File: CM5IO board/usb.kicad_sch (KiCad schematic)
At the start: 0 parts

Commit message: Duplicated additional USB-C in sch.
How to change pin label on CM5?
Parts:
- added D5: SP0503BAHT, Package_TO_SOT_SMD:SOT-143, symbol Power_Protection:SP0503BAHT
- added J9: USB_C_Receptacle_USB2.0, iclr:USB_C_Receptacle_Palconn_UTC16-G, symbol Connector:USB_C_Receptacle_USB2.0
- added LED6: WHITE_LED, LED_SMD:LED_0402_1005Metric, symbol Device:LED_Small
- added R24, R25, R26: 5.1k, Resistor_SMD:R_0402_1005Metric, symbol Device:R_Small
- added TP6, TP7: TestPoint, TestPoint:TestPoint_Pad_D1.0mm, symbol Connector:TestPoint
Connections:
- new net: LED6.2 (A), R26.2
- new net: J9.B5 (CC2), R25.2
- new net: J9.A5 (CC1), R24.1
- new net Data+: D5.4 (K), J9.A6 (D+), J9.B6 (D+), TP7.1
- new net Data-: D5.3 (K), J9.A7 (D-), J9.B7 (D-), TP6.1
- new net GND: D5.1 (A), J9.A1 (GND), J9.A12 (GND), J9.B1 (GND), J9.B12 (GND), J9.S1 (SHIELD), LED6.1 (K), R24.2, R25.1
- new net VBUS: D5.2 (K), J9.A4 (VBUS), J9.A9 (VBUS), J9.B4 (VBUS), J9.B9 (VBUS), R26.1
- no-connect marks 0 -> 2

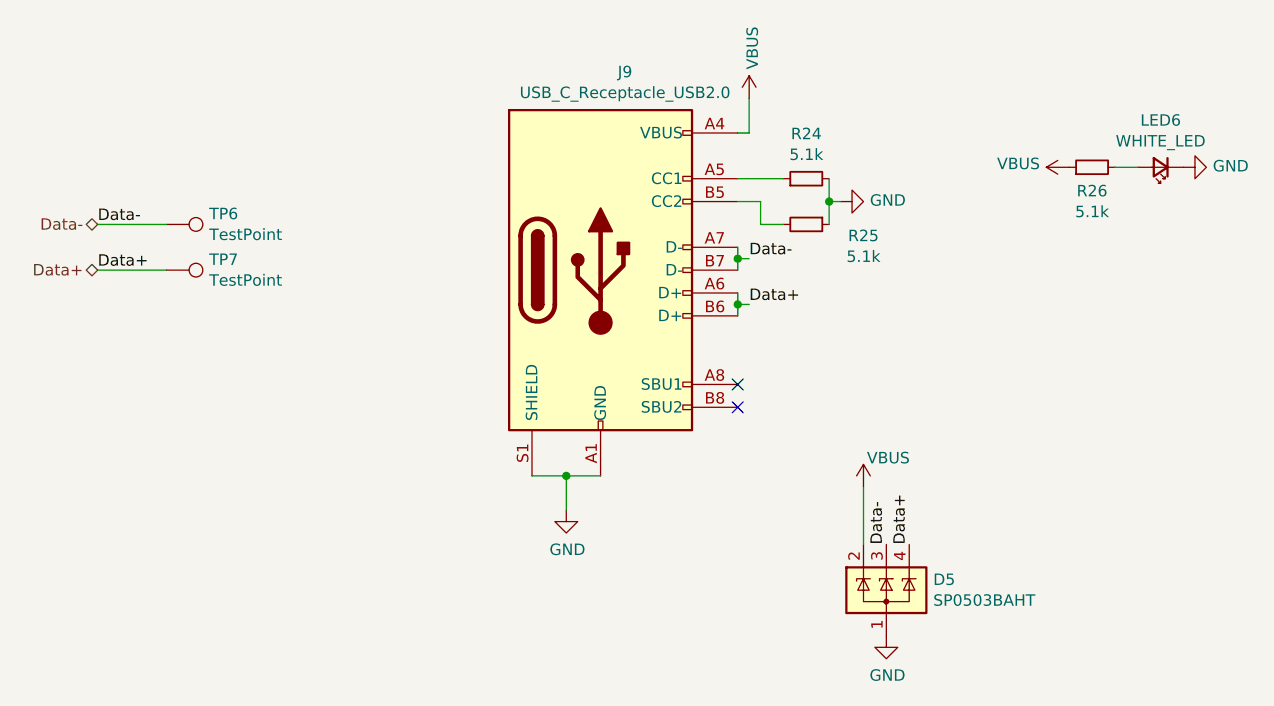
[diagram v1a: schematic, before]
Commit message: Moved Ricardo to hierarchical sheet in main sch.
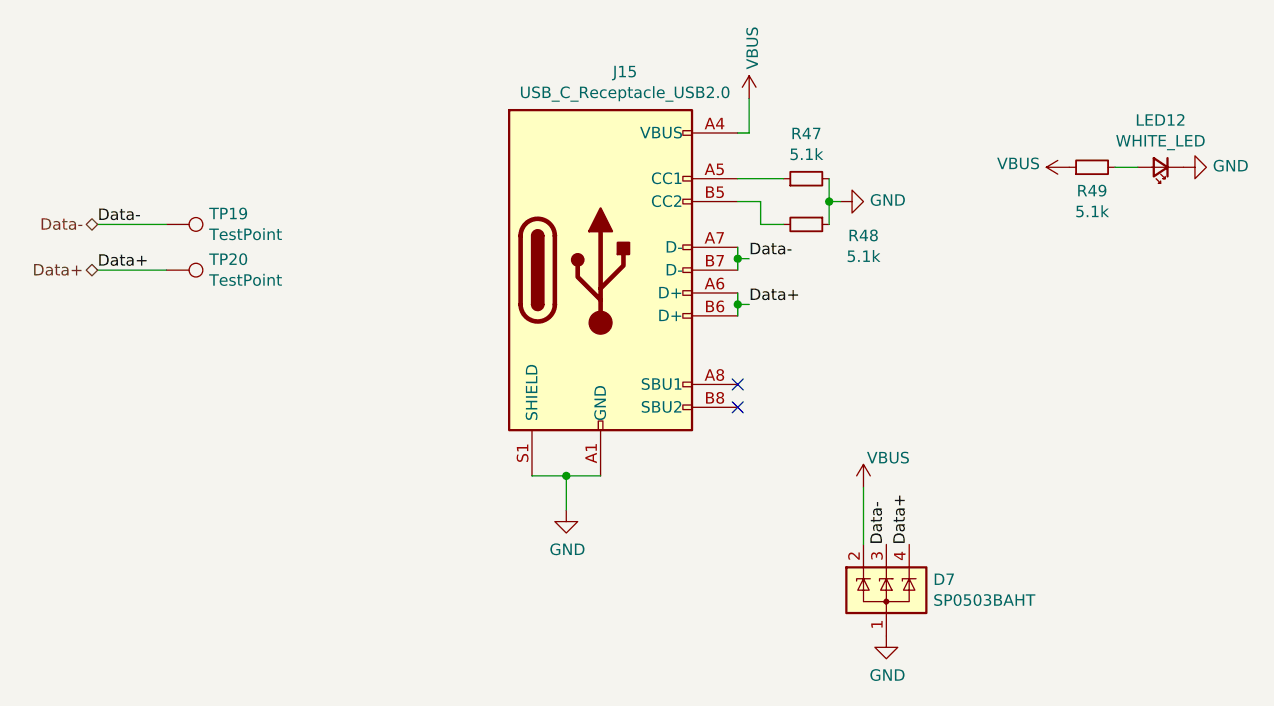
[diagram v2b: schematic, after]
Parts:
- renumbered D5 to D7, J9 to J15, LED6 to LED12, R24 to R47, R25 to R48, R26 to R49, TP6 to TP19, TP7 to TP20
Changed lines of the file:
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@@
 		(on_board yes)
 		(dnp no)
-		(property "Reference" "LED6"
+		(property "Reference" "LED12"
 			(at 196.85 68.453 0)
 			(effects
@@
 		(instances
 			(project "CM5IO"
-				(path "/e63e39d7-6ac0-4ffd-8aa3-1841a4541b55/c862b160-a356-459e-a62e-d71f5db5c7f5"
-					(reference "LED6")
+				(path "/e63e39d7-6ac0-4ffd-8aa3-1841a4541b55/9fe0f7c3-d1a2-46ee-9d93-86ad4b786b0e/0c984a55-4862-4f62-828e-8c31ecb6e4fe"
+					(reference "LED12")
 					(unit 1)
 				)
@@
 		(on_board yes)
 		(dnp no)
-		(property "Reference" "#PWR055"
+		(property "Reference" "#PWR0125"
 			(at 167.64 77.47 0)
 			(effects
@@
 		(instances
 			(project "CM5IO"
-				(path "/e63e39d7-6ac0-4ffd-8aa3-1841a4541b55/c862b160-a356-459e-a62e-d71f5db5c7f5"
-					(reference "#PWR055")
+				(path "/e63e39d7-6ac0-4ffd-8aa3-1841a4541b55/9fe0f7c3-d1a2-46ee-9d93-86ad4b786b0e/0c984a55-4862-4f62-828e-8c31ecb6e4fe"
+					(reference "#PWR0125")
 					(unit 1)
 				)
@@
 		(on_board yes)
 		(dnp no)
-		(property "Reference" "R25"
+		(property "Reference" "R48"
 			(at 163.83 81.28 90)
 			(effects
@@
 		(instances
 			(project "CM5IO"
-				(path "/e63e39d7-6ac0-4ffd-8aa3-1841a4541b55/c862b160-a356-459e-a62e-d71f5db5c7f5"
-					(reference "R25")
+				(path "/e63e39d7-6ac0-4ffd-8aa3-1841a4541b55/9fe0f7c3-d1a2-46ee-9d93-86ad4b786b0e/0c984a55-4862-4f62-828e-8c31ecb6e4fe"
+					(reference "R48")
 					(unit 1)
 				)
@@
 		(on_board yes)
 		(dnp no)
-		(property "Reference" "#PWR057"
+		(property "Reference" "#PWR0127"
 			(at 166.37 132.08 0)
 			(effects
@@
 		(instances
 			(project "CM5IO"
-				(path "/e63e39d7-6ac0-4ffd-8aa3-1841a4541b55/c862b160-a356-459e-a62e-d71f5db5c7f5"
-					(reference "#PWR057")
+				(path "/e63e39d7-6ac0-4ffd-8aa3-1841a4541b55/9fe0f7c3-d1a2-46ee-9d93-86ad4b786b0e/0c984a55-4862-4f62-828e-8c31ecb6e4fe"
+					(reference "#PWR0127")
 					(unit 1)
 				)
@@
 		(on_board yes)
 		(dnp no)
-		(property "Reference" "#PWR054"
+		(property "Reference" "#PWR0124"
 			(at 151.13 69.85 0)
 			(effects
@@
 		(instances
 			(project "CM5IO"
-				(path "/e63e39d7-6ac0-4ffd-8aa3-1841a4541b55/c862b160-a356-459e-a62e-d71f5db5c7f5"
-					(reference "#PWR054")
+				(path "/e63e39d7-6ac0-4ffd-8aa3-1841a4541b55/9fe0f7c3-d1a2-46ee-9d93-86ad4b786b0e/0c984a55-4862-4f62-828e-8c31ecb6e4fe"
+					(reference "#PWR0124")
 					(unit 1)
 				)
@@
 		(on_board yes)
 		(dnp no)
-		(property "Reference" "#PWR053"
+		(property "Reference" "#PWR0123"
 			(at 130.81 118.11 0)
 			(effects
@@
 		(instances
 			(project "CM5IO"
-				(path "/e63e39d7-6ac0-4ffd-8aa3-1841a4541b55/c862b160-a356-459e-a62e-d71f5db5c7f5"
-					(reference "#PWR053")
+				(path "/e63e39d7-6ac0-4ffd-8aa3-1841a4541b55/9fe0f7c3-d1a2-46ee-9d93-86ad4b786b0e/0c984a55-4862-4f62-828e-8c31ecb6e4fe"
+					(reference "#PWR0123")
 					(unit 1)
 				)
@@
 		(on_board yes)
 		(dnp no)
-		(property "Reference" "J9"
+		(property "Reference" "J15"
 			(at 137.3378 63.0682 0)
 			(effects
@@
 		(instances
 			(project "CM5IO"
-				(path "/e63e39d7-6ac0-4ffd-8aa3-1841a4541b55/c862b160-a356-459e-a62e-d71f5db5c7f5"
-					(reference "J9")
+				(path "/e63e39d7-6ac0-4ffd-8aa3-1841a4541b55/9fe0f7c3-d1a2-46ee-9d93-86ad4b786b0e/0c984a55-4862-4f62-828e-8c31ecb6e4fe"
+					(reference "J15")
 					(unit 1)
 				)
@@
 		(on_board yes)
 		(dnp no)
-		(property "Reference" "TP6"
+		(property "Reference" "TP19"
 			(at 91.1352 78.8416 90)
 			(effects
@@
 		(instances
 			(project "CM5IO"
-				(path "/e63e39d7-6ac0-4ffd-8aa3-1841a4541b55/c862b160-a356-459e-a62e-d71f5db5c7f5"
-					(reference "TP6")
+				(path "/e63e39d7-6ac0-4ffd-8aa3-1841a4541b55/9fe0f7c3-d1a2-46ee-9d93-86ad4b786b0e/0c984a55-4862-4f62-828e-8c31ecb6e4fe"
+					(reference "TP19")
 					(unit 1)
 				)
@@
 		(on_board yes)
 		(dnp no)
-		(property "Reference" "#PWR056"
+		(property "Reference" "#PWR0126"
 			(at 163.83 113.03 0)
 			(effects
@@
 		(instances
 			(project "CM5IO"
-				(path "/e63e39d7-6ac0-4ffd-8aa3-1841a4541b55/c862b160-a356-459e-a62e-d71f5db5c7f5"
-					(reference "#PWR056")
+				(path "/e63e39d7-6ac0-4ffd-8aa3-1841a4541b55/9fe0f7c3-d1a2-46ee-9d93-86ad4b786b0e/0c984a55-4862-4f62-828e-8c31ecb6e4fe"
+					(reference "#PWR0126")
 					(unit 1)
 				)
@@
 		(on_board yes)
 		(dnp no)
-		(property "Reference" "TP7"
+		(property "Reference" "TP20"
 			(at 91.1352 83.9216 90)
 			(effects
@@
 		(instances
 			(project "CM5IO"
-				(path "/e63e39d7-6ac0-4ffd-8aa3-1841a4541b55/c862b160-a356-459e-a62e-d71f5db5c7f5"
-					(reference "TP7")
+				(path "/e63e39d7-6ac0-4ffd-8aa3-1841a4541b55/9fe0f7c3-d1a2-46ee-9d93-86ad4b786b0e/0c984a55-4862-4f62-828e-8c31ecb6e4fe"
+					(reference "TP20")
 					(unit 1)
 				)
@@
 		(on_board yes)
 		(dnp no)
-		(property "Reference" "D5"
+		(property "Reference" "D7"
 			(at 171.577 119.4816 0)
 			(effects
@@
 		(instances
 			(project "CM5IO"
-				(path "/e63e39d7-6ac0-4ffd-8aa3-1841a4541b55/c862b160-a356-459e-a62e-d71f5db5c7f5"
-					(reference "D5")
+				(path "/e63e39d7-6ac0-4ffd-8aa3-1841a4541b55/9fe0f7c3-d1a2-46ee-9d93-86ad4b786b0e/0c984a55-4862-4f62-828e-8c31ecb6e4fe"
+					(reference "D7")
 					(unit 1)
 				)
@@
 		(on_board yes)
 		(dnp no)
-		(property "Reference" "#PWR058"
+		(property "Reference" "#PWR0128"
 			(at 190.5 73.66 0)
 			(effects
@@
 		(instances
 			(project "CM5IO"
-				(path "/e63e39d7-6ac0-4ffd-8aa3-1841a4541b55/c862b160-a356-459e-a62e-d71f5db5c7f5"
-					(reference "#PWR058")
+				(path "/e63e39d7-6ac0-4ffd-8aa3-1841a4541b55/9fe0f7c3-d1a2-46ee-9d93-86ad4b786b0e/0c984a55-4862-4f62-828e-8c31ecb6e4fe"
+					(reference "#PWR0128")
 					(unit 1)
 				)
@@
 		(on_board yes)
 		(dnp no)
-		(property "Reference" "R24"
+		(property "Reference" "R47"
 			(at 157.48 69.9516 90)
 			(effects
@@
 		(instances
 			(project "CM5IO"
-				(path "/e63e39d7-6ac0-4ffd-8aa3-1841a4541b55/c862b160-a356-459e-a62e-d71f5db5c7f5"
-					(reference "R24")
+				(path "/e63e39d7-6ac0-4ffd-8aa3-1841a4541b55/9fe0f7c3-d1a2-46ee-9d93-86ad4b786b0e/0c984a55-4862-4f62-828e-8c31ecb6e4fe"
+					(reference "R47")
 					(unit 1)
 				)
@@
 		(on_board yes)
 		(dnp no)
-		(property "Reference" "R26"
+		(property "Reference" "R49"
 			(at 189.23 76.3016 90)
 			(effects
@@
 		(instances
 			(project "CM5IO"
-				(path "/e63e39d7-6ac0-4ffd-8aa3-1841a4541b55/c862b160-a356-459e-a62e-d71f5db5c7f5"
-					(reference "R26")
+				(path "/e63e39d7-6ac0-4ffd-8aa3-1841a4541b55/9fe0f7c3-d1a2-46ee-9d93-86ad4b786b0e/0c984a55-4862-4f62-828e-8c31ecb6e4fe"
+					(reference "R49")
 					(unit 1)
 				)
@@
 		(on_board yes)
 		(dnp no)
-		(property "Reference" "#PWR059"
+		(property "Reference" "#PWR0129"
 			(at 205.74 73.66 0)
 			(effects
@@
 		(instances
 			(project "CM5IO"
-				(path "/e63e39d7-6ac0-4ffd-8aa3-1841a4541b55/c862b160-a356-459e-a62e-d71f5db5c7f5"
-					(reference "#PWR059")
-					(unit 1)
-				)
+				(path "/e63e39d7-6ac0-4ffd-8aa3-1841a4541b55/9fe0f7c3-d1a2-46ee-9d93-86ad4b786b0e/0c984a55-4862-4f62-828e-8c31ecb6e4fe"
+					(reference "#PWR0129")
+					(unit 1)
+				)
